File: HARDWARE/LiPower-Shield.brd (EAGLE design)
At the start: 59.7 x 53.3 mm, 42 parts, among them U1 MAX17043G+U, U2 TPS61200, U3 MCP73831, U4 ARDUINO_SHIELDNOLABELS, X1 USBSMD

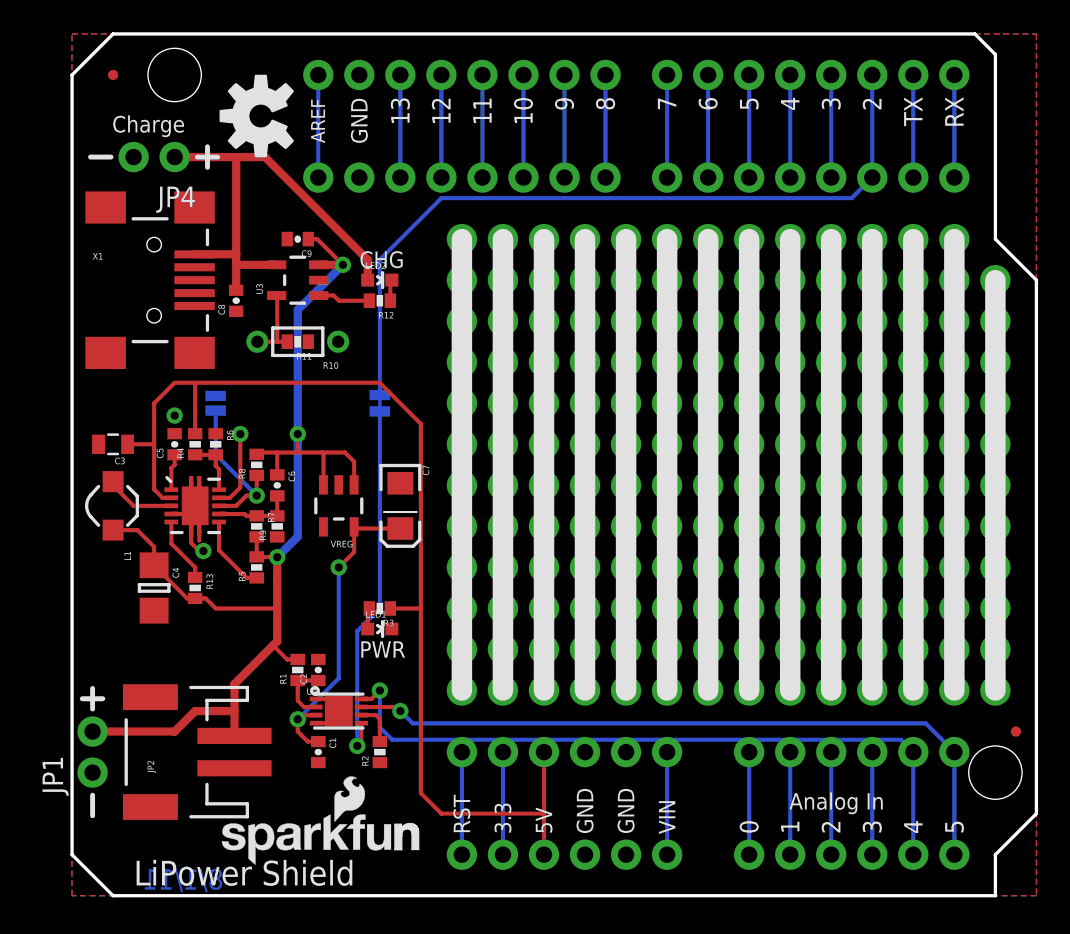
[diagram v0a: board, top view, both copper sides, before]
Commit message: Had to re-commit original files
The v13 files that I pulled from the network are not what we have on
storefront. commited v12,  also from the network, seems to be the same
as the SF product.
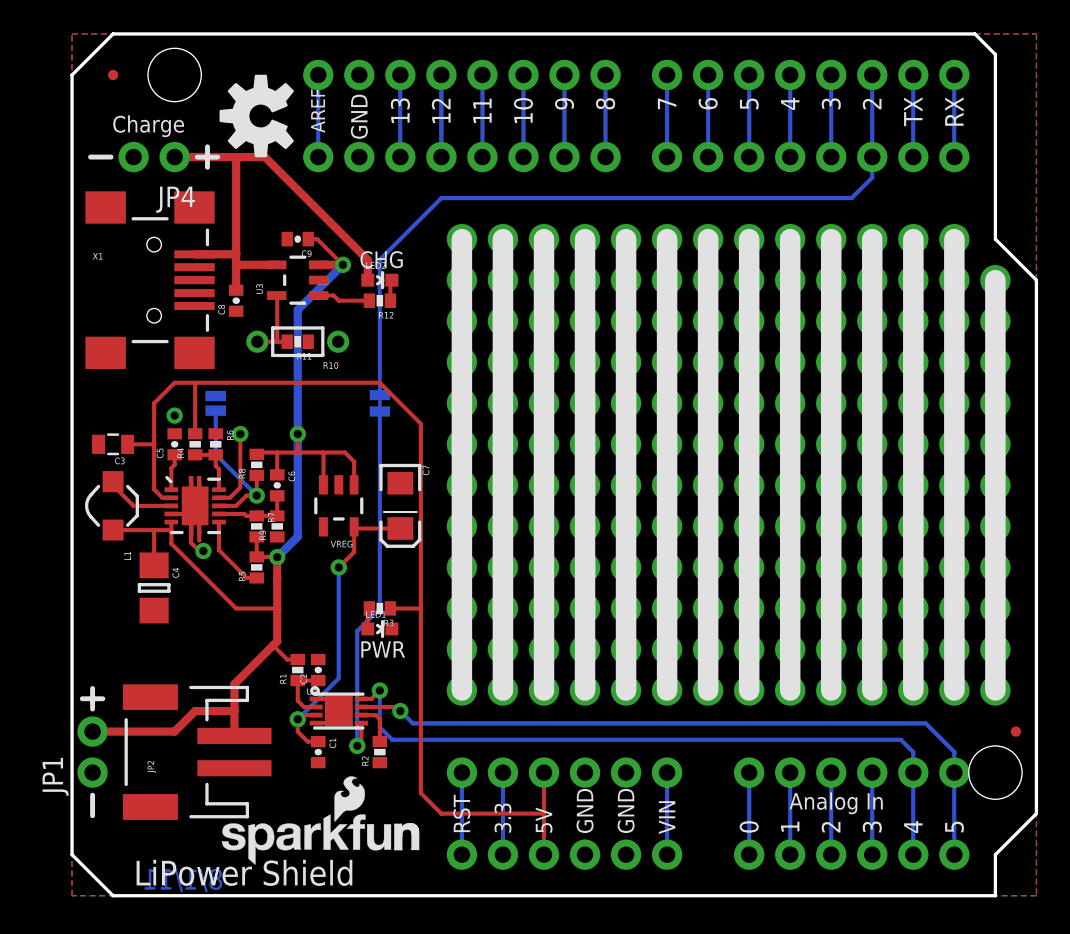
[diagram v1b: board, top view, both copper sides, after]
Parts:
- removed R13: 100, SparkFun:0402-RES
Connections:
- removed net VIN-L: R13.1, U2.5
- net VBATT: now also U2.5; no longer R13.2
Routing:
- net VIN-L: track 4.04 -> 0.00 mm
- net VBATT: track 75.3 -> 77.8 mm
- net VIN: track 6.35 -> 5.08 mm
- net RST: track 6.35 -> 5.08 mm
- net A3: track 6.35 -> 5.08 mm
- net A2: track 6.35 -> 5.08 mm
- net A1: track 6.35 -> 5.08 mm
- net A0: track 6.35 -> 5.08 mm
- net 3.3-ARDUINO: track 6.35 -> 5.08 mm
- net TX: track 6.35 -> 5.08 mm
- net RX: track 6.35 -> 5.08 mm
- net D9: track 6.35 -> 5.08 mm
- net D8: track 6.35 -> 5.08 mm
- net D7: track 6.35 -> 5.08 mm
- net D6: track 6.35 -> 5.08 mm
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
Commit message: re-up
Re Committed the original files.
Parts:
- moved JP6 6.16 mm to (56.9, 4.19)
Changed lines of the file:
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@@
 <?xml version="1.0" encoding="utf-8"?>
 <!DOCTYPE eagle SYSTEM "eagle.dtd">
-<eagle version="6.4">
+<eagle version="6.5.0">
 <drawing>
 <settings>
@@
 <text x="51.4985" y="49.4665" size="1.143" layer="21" font="vector" ratio="15" rot="R270">TX</text>
 <text x="54.0385" y="49.4665" size="1.143" layer="21" font="vector" ratio="15" rot="R270">RX</text>
-<text x="24.638" y="3.81" size="1.016" layer="21" font="vector" ratio="15" rot="R90">RST</text>
-<text x="32.258" y="3.81" size="1.016" layer="21" font="vector" ratio="15" rot="R90">GND</text>
-<text x="27.178" y="3.81" size="1.016" layer="21" font="vector" ratio="15" rot="R90">3.3</text>
-<text x="29.718" y="3.81" size="1.016" layer="21" font="vector" ratio="15" rot="R90">5V</text>
-<text x="34.798" y="3.81" size="1.016" layer="21" font="vector" ratio="15" rot="R90">GND</text>
-<text x="37.338" y="3.81" size="1.016" layer="21" font="vector" ratio="15" rot="R90">VIN</text>
-<text x="44.3865" y="5.334" size="1.016" layer="21" font="vector" ratio="15">Analog In</text>
-<text x="42.4815" y="3.81" size="1.143" layer="21" font="vector" ratio="15" rot="R90">0</text>
-<text x="45.0215" y="3.81" size="1.143" layer="21" font="vector" ratio="15" rot="R90">1</text>
-<text x="47.5615" y="3.81" size="1.143" layer="21" font="vector" ratio="15" rot="R90">2</text>
-<text x="50.1015" y="3.81" size="1.143" layer="21" font="vector" ratio="15" rot="R90">3</text>
-<text x="52.6415" y="3.81" size="1.143" layer="21" font="vector" ratio="15" rot="R90">4</text>
-<text x="55.1815" y="3.81" size="1.143" layer="21" font="vector" ratio="15" rot="R90">5</text>
+<text x="24.638" y="4.064" size="1.016" layer="21" font="vector" ratio="15" rot="R90">RST</text>
+<text x="32.258" y="4.064" size="1.016" layer="21" font="vector" ratio="15" rot="R90">GND</text>
+<text x="27.178" y="4.064" size="1.016" layer="21" font="vector" ratio="15" rot="R90">3.3</text>
+<text x="29.718" y="4.064" size="1.016" layer="21" font="vector" ratio="15" rot="R90">5V</text>
+<text x="34.798" y="4.064" size="1.016" layer="21" font="vector" ratio="15" rot="R90">GND</text>
+<text x="37.338" y="4.064" size="1.016" layer="21" font="vector" ratio="15" rot="R90">VIN</text>
+<text x="44.3865" y="5.588" size="1.016" layer="21" font="vector" ratio="15">Analog In</text>
+<text x="42.4815" y="3.937" size="1.143" layer="21" font="vector" ratio="15" rot="R90">0</text>
+<text x="45.0215" y="4.064" size="1.143" layer="21" font="vector" ratio="15" rot="R90">1</text>
+<text x="47.5615" y="3.937" size="1.143" layer="21" font="vector" ratio="15" rot="R90">2</text>
+<text x="50.1015" y="3.937" size="1.143" layer="21" font="vector" ratio="15" rot="R90">3</text>
+<text x="52.6415" y="3.937" size="1.143" layer="21" font="vector" ratio="15" rot="R90">4</text>
+<text x="55.1815" y="3.937" size="1.143" layer="21" font="vector" ratio="15" rot="R90">5</text>
 <text x="17.653" y="32.004" size="1.016" layer="22" font="vector" ratio="15" rot="MR270">ALT</text>
 <text x="21.336" y="31.496" size="1.016" layer="22" font="vector" ratio="15" rot="MR270">D2</text>
@@
 <element name="SJ2" library="SparkFun" package="SJ_2S-NO" value="PS" x="8.89" y="30.48" rot="MR270"/>
 <element name="JP5" library="abes" package="FIDUCIAL-1X2.5" value="FIDUCIAL1X2.5" x="2.54" y="50.8"/>
-<element name="JP6" library="abes" package="FIDUCIAL-1X2.5" value="FIDUCIAL1X2.5" x="58.42" y="10.16"/>
+<element name="JP6" library="abes" package="FIDUCIAL-1X2.5" value="FIDUCIAL1X2.5" x="56.896" y="4.191"/>
 </elements>
 <signals>
